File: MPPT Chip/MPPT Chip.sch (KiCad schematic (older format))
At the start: 2 parts, among them J1 Conn_02x05_Counter_Clockwise, U0 MAX20801

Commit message: 11/10 meeting updates
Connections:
- net GND: now reaches J1.3 (Pin_3), U0.3 (GND1)
- net GND: now also J1.4 (Pin_4), J1.7 (Pin_7), U0.4 (GND2), U0.7 (GND3)
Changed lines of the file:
@@
 	5300 5000 5650 5000
-Wire Wire Line
-	5550 3800 5250 3800
 Wire Wire Line
 	5250 3800 5250 5100
@@
 	5250 5100 5650 5100
 Wire Wire Line
-	5550 3900 5200 3900
-Wire Wire Line
 	5200 3900 5200 5200
 Wire Wire Line
 	5200 5200 5650 5200
-Wire Wire Line
-	5550 4000 5150 4000
 Wire Wire Line
 	5150 4000 5150 5300
@@
 	5550 4150 5550 4550
 Wire Wire Line
-	5550 4550 6650 4550
-Wire Wire Line
 	6650 4550 6650 5200
 Wire Wire Line
@@
 Wire Wire Line
 	7000 4900 6150 4900
+$Comp
+L power:GND #PWR?
+U 1 1 618833C8
+P 5450 5600
+F 0 "#PWR?" H 5450 5350 50  0001 C CNN
+F 1 "GND" H 5455 5427 50  0000 C CNN
+F 2 "" H 5450 5600 50  0001 C CNN
+F 3 "" H 5450 5600 50  0001 C CNN
+	1    5450 5600
+	1    0    0    -1
+$EndComp
+Wire Wire Line
+	5550 4000 5150 4000
+Wire Wire Line
+	5550 3900 5500 3900
+Wire Wire Line
+	5550 3800 5450 3800
+Wire Wire Line
+	5500 3900 5500 5600
+Wire Wire Line
+	5500 5600 5450 5600
+Connection ~ 5500 3900
+Wire Wire Line
+	5500 3900 5200 3900
+Wire Wire Line
+	5450 3800 5450 5600
+Connection ~ 5450 3800
+Wire Wire Line
+	5450 3800 5250 3800
+Connection ~ 5450 5600
+Wire Wire Line
+	5550 4550 5600 4550
+Wire Wire Line
+	5600 4550 5600 5600
+Wire Wire Line
+	5600 5600 5500 5600
+Connection ~ 5600 4550
+Wire Wire Line
+	5600 4550 6650 4550
+Connection ~ 5500 5600
+Text Label 5800 4550 0    50   ~ 0
+GND
 $EndSCHEMATC

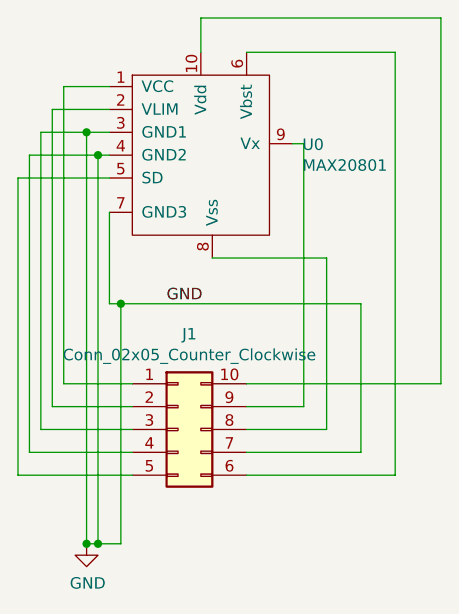
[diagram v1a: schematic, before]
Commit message: v2 fix based off of durfee review
messed up connections, tried to fix
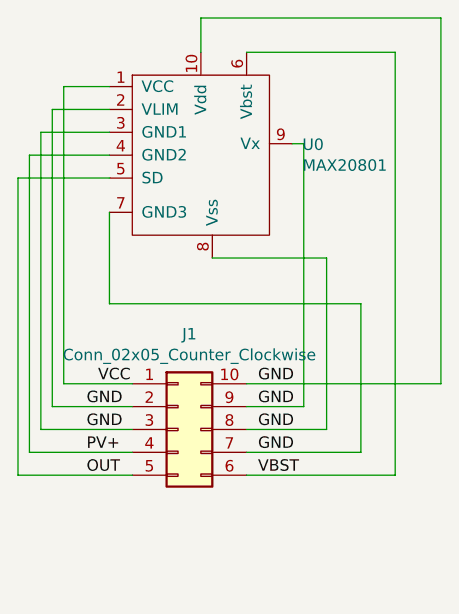
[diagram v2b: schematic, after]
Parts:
- J1: footprint MAX20801:PinHeader -> Connector_PinHeader_2.54mm:BSE_Connector
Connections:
- net GND: now also J1.10 (Pin_10), J1.2 (Pin_2), J1.8 (Pin_8), J1.9 (Pin_9), U0.10 (Vdd), U0.2 (VLIM), U0.8 (Vss), U0.9 (Vx); no longer J1.4 (Pin_4), U0.4 (GND2)
- net VCC: now reaches J1.1 (Pin_1), U0.1 (VCC)
- net OUT: now reaches J1.5 (Pin_5), U0.5 (SD)
- net VBST: now reaches J1.6 (Pin_6), U0.6 (Vbst)
- new net PV+: J1.4 (Pin_4), U0.4 (GND2)
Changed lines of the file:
@@
 Comment4 ""
 $EndDescr
-$Comp
-L Connector_Generic:Conn_02x05_Counter_Clockwise J1
-U 1 1 617A6B1C
-P 5850 5100
-F 0 "J1" H 5900 5517 50  0000 C CNN
-F 1 "Conn_02x05_Counter_Clockwise" H 5900 5426 50  0000 C CNN
-F 2 "MAX20801:PinHeader" H 5850 5100 50  0001 C CNN
-F 3 "~" H 5850 5100 50  0001 C CNN
-	1    5850 5100
-	1    0    0    -1
-$EndComp
-$Comp
-L MAX20801:MAX20801 U0
-U 1 1 6163421A
-P 5900 4150
-F 0 "U0" H 6394 4446 50  0000 L CNN
-F 1 "MAX20801" H 6394 4355 50  0000 L CNN
-F 2 "MAX20801:MAX20801" H 5900 4150 50  0001 C CNN
-F 3 "" H 5900 4150 50  0001 C CNN
-	1    5900 4150
-	1    0    0    -1
-$EndComp
-Wire Wire Line
-	5550 3600 5350 3600
-Wire Wire Line
-	5350 3600 5350 4900
-Wire Wire Line
-	5350 4900 5650 4900
-Wire Wire Line
-	5550 3700 5300 3700
-Wire Wire Line
-	5300 3700 5300 5000
-Wire Wire Line
-	5300 5000 5650 5000
-Wire Wire Line
-	5250 3800 5250 5100
-Wire Wire Line
-	5250 5100 5650 5100
-Wire Wire Line
-	5200 3900 5200 5200
-Wire Wire Line
-	5200 5200 5650 5200
-Wire Wire Line
-	5150 4000 5150 5300
-Wire Wire Line
-	5150 5300 5650 5300
 Wire Wire Line
 	6150 3450 6800 3450
@@
 	6500 5100 6150 5100
 Wire Wire Line
-	5550 4150 5550 4550
-Wire Wire Line
 	6650 4550 6650 5200
 Wire Wire Line
@@
 Wire Wire Line
 	6400 3850 6350 3850
-Wire Wire Line
-	6400 3850 6400 5000
 Wire Wire Line
 	6400 5000 6150 5000
@@
 Wire Wire Line
 	7000 4900 6150 4900
+Wire Wire Line
+	6400 3850 6400 5000
+Wire Wire Line
+	5550 4000 5150 4000
+Wire Wire Line
+	5550 4150 5550 4550
+Wire Wire Line
+	5150 5300 5650 5300
+Wire Wire Line
+	5150 4000 5150 5300
+Wire Wire Line
+	5200 5200 5650 5200
+Wire Wire Line
+	5200 3900 5200 5200
+Wire Wire Line
+	5250 5100 5650 5100
+Wire Wire Line
+	5250 3800 5250 5100
+Wire Wire Line
+	5300 5000 5650 5000
+Wire Wire Line
+	5300 3700 5300 5000
+Wire Wire Line
+	5550 3700 5300 3700
+Wire Wire Line
+	5350 4900 5650 4900
+Wire Wire Line
+	5350 3600 5350 4900
+Wire Wire Line
+	5550 3600 5350 3600
 $Comp
-L power:GND #PWR?
-U 1 1 618833C8
-P 5450 5600
-F 0 "#PWR?" H 5450 5350 50  0001 C CNN
-F 1 "GND" H 5455 5427 50  0000 C CNN
-F 2 "" H 5450 5600 50  0001 C CNN
-F 3 "" H 5450 5600 50  0001 C CNN
-	1    5450 5600
+L MAX20801:MAX20801 U0
+U 1 1 6163421A
+P 5900 4150
+F 0 "U0" H 6394 4446 50  0000 L CNN
+F 1 "MAX20801" H 6394 4355 50  0000 L CNN
+F 2 "MAX20801:MAX20801" H 5900 4150 50  0001 C CNN
+F 3 "" H 5900 4150 50  0001 C CNN
+	1    5900 4150
+	1    0    0    -1
+$EndComp
+$Comp
+L Connector_Generic:Conn_02x05_Counter_Clockwise J1
+U 1 1 617A6B1C
+P 5850 5100
+F 0 "J1" H 5900 5517 50  0000 C CNN
+F 1 "Conn_02x05_Counter_Clockwise" H 5900 5426 50  0000 C CNN
+F 2 "Connector_PinHeader_2.54mm:BSE_Connector" H 5850 5100 50  0001 C CNN
+F 3 "~" H 5850 5100 50  0001 C CNN
+	1    5850 5100
 	1    0    0    -1
 $EndComp
 Wire Wire Line
-	5550 4000 5150 4000
+	5550 4550 6650 4550
 Wire Wire Line
-	5550 3900 5500 3900
+	5250 3800 5550 3800
 Wire Wire Line
-	5550 3800 5450 3800
-Wire Wire Line
-	5500 3900 5500 5600
-Wire Wire Line
-	5500 5600 5450 5600
-Connection ~ 5500 3900
-Wire Wire Line
-	5500 3900 5200 3900
-Wire Wire Line
-	5450 3800 5450 5600
-Connection ~ 5450 3800
-Wire Wire Line
-	5450 3800 5250 3800
-Connection ~ 5450 5600
-Wire Wire Line
-	5550 4550 5600 4550
-Wire Wire Line
-	5600 4550 5600 5600
-Wire Wire Line
-	5600 5600 5500 5600
-Connection ~ 5600 4550
-Wire Wire Line
-	5600 4550 6650 4550
-Connection ~ 5500 5600
-Text Label 5800 4550 0    50   ~ 0
+	5200 3900 5550 3900
+Text Label 5500 4900 0    50   ~ 0
+VCC
+Text Label 5450 5000 0    50   ~ 0
+GND
+Text Label 5450 5200 0    50   ~ 0
+PV+
+Text Label 5450 5300 0    50   ~ 0
+OUT
+Text Label 6200 4900 0    50   ~ 0
+GND
+Text Label 6200 5000 0    50   ~ 0
+GND
+Text Label 6200 5100 0    50   ~ 0
+GND
+Text Label 6200 5200 0    50   ~ 0
+GND
+Text Label 6200 5300 0    50   ~ 0
+VBST
+Text Label 5450 5100 0    50   ~ 0
 GND
 $EndSCHEMATC
